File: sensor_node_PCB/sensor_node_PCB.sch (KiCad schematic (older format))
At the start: 37 parts, among them J1 USB_B_Mini, J3 OUTPUT_CONNECTOR, P1 BREAKOUTS, Q1 FDN340P, Q2 BSS138, Q3 BSS138, U1 LMV358IDGKR, U10 dps310, U2 LD1117S50TR, U4 LM1117-3.3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

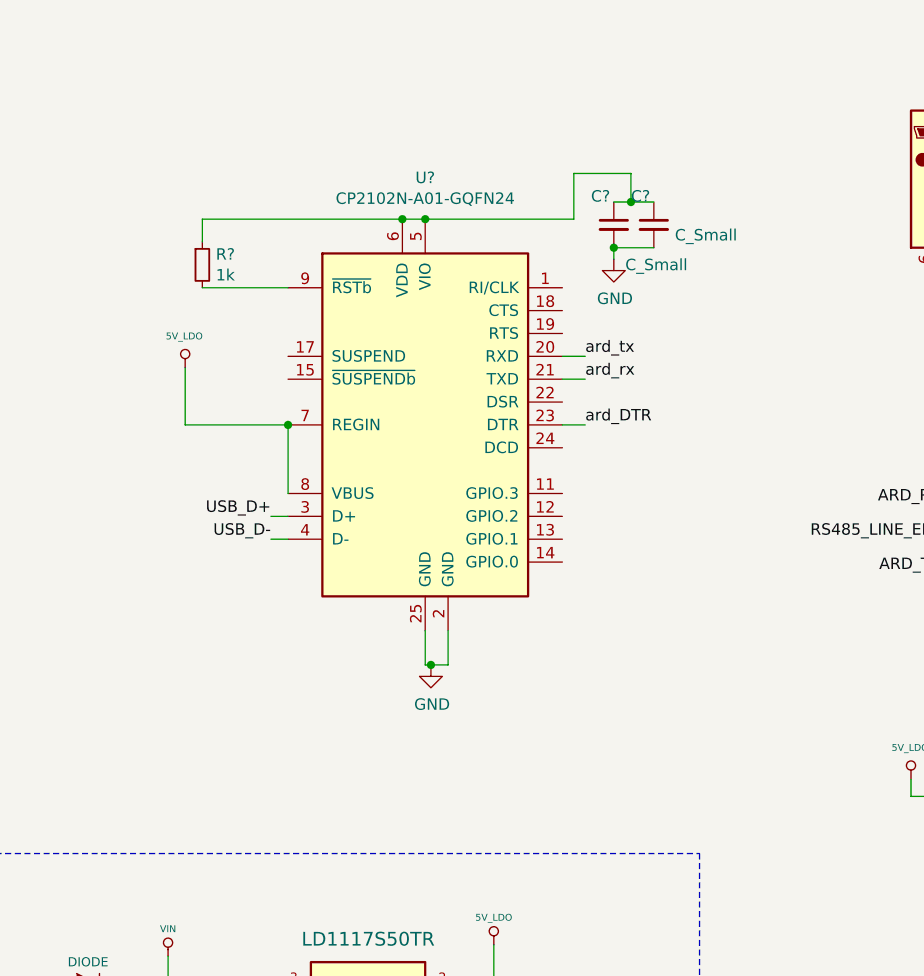
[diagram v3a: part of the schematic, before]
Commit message: changed cp2102 to 28 pin version
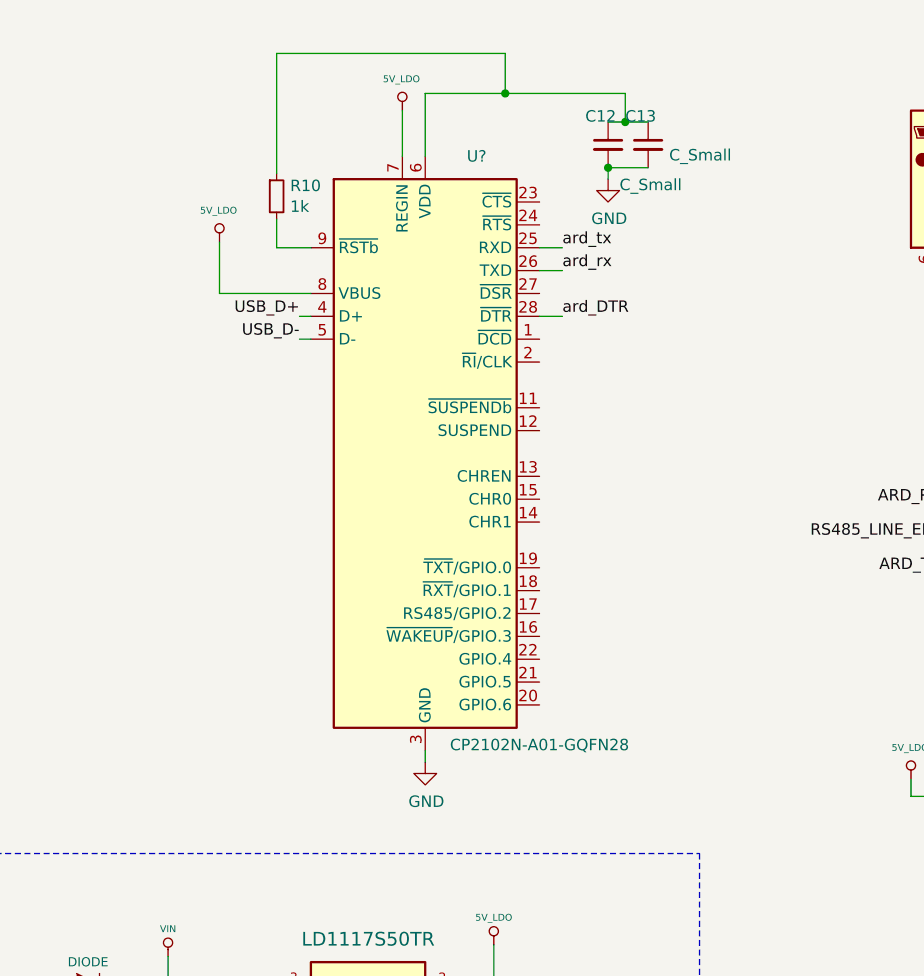
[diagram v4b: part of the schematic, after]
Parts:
- removed U?: CP2102N-A01-GQFN24, Package_DFN_QFN:QFN-24-1EP_4x4mm_P0.5mm_EP2.6x2.6mm, symbol Interface_USB:CP2102N-A01-GQFN24
- added U?: CP2102N-A01-GQFN28, Package_DFN_QFN:QFN-28-1EP_5x5mm_P0.5mm_EP3.35x3.35mm, symbol Interface_USB:CP2102N-A01-GQFN28
- C12, C13: renamed from C?; footprint (none) -> Capacitor_SMD:C_0603_1608Metric
- R10: renamed from R?; footprint (none) -> Resistor_SMD:R_0603_1608Metric
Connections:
- net 5V_LDO: now also U?.7 (REGIN), U?.8 (VBUS)
- net GND: now also U?.29 (GND), U?.3 (GND)
- net USB_D+: now also U?.4 (D+)
- net USB_D-: now also U?.5 (D-)
- net ard_DTR: now also U?.28 (~DTR)
- net ard_rx: now also U?.26 (TXD)
- net ard_tx: now also U?.25 (RXD)
- net at C12.1, C13.1, R10.1: now also U?.6 (VDD)
- net at R10.2: now also U?.9 (~RSTb)
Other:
- moved on the sheet: C12, C13, R10
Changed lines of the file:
@@
 Text GLabel 1800 4725 0    50   Input ~ 0
 12V_BUS
-Text Label 3275 2675 2    50   ~ 0
+Text Label 3400 1800 2    50   ~ 0
 USB_D+
-Text Label 3275 2775 2    50   ~ 0
+Text Label 3400 1900 2    50   ~ 0
 USB_D-
 Text Label 1425 3150 0    50   ~ 0
@@
 Wire Wire Line
 	1350 3250 1425 3250
-Text Label 4650 1975 0    50   ~ 0
+Text Label 4550 1500 0    50   ~ 0
 ard_tx
-Text Label 4650 2075 0    50   ~ 0
+Text Label 4550 1600 0    50   ~ 0
 ard_rx
 Text Label 1450 3050 0    50   ~ 0
 ard_DTR
-Text Label 4650 2275 0    50   ~ 0
+Text Label 4550 1800 0    50   ~ 0
 ard_DTR
-$Comp
-L Arduino_Uno_R3_From_Scratch-rescue:GND #PWR0112
-U 1 1 5F50BD57
-P 3975 3325
-F 0 "#PWR0112" H 3975 3075 50  0001 C CNN
-F 1 "GND" H 3980 3152 50  0000 C CNN
-F 2 "" H 3975 3325 60  0000 C CNN
-F 3 "" H 3975 3325 60  0000 C CNN
-	1    3975 3325
-	1    0    0    -1
-$EndComp
 Text Label 1425 2675 0    50   ~ 0
 ARD_TX1
@@
 Connection ~ 7075 5600
 $Comp
-L Interface_USB:CP2102N-A01-GQFN24 U?
-U 1 1 5FEADE93
-P 3950 2275
-F 0 "U?" H 3950 3356 50  0000 C CNN
-F 1 "CP2102N-A01-GQFN24" H 3950 3265 50  0000 C CNN
-F 2 "Package_DFN_QFN:QFN-24-1EP_4x4mm_P0.5mm_EP2.6x2.6mm" H 4400 1475 50  0001 L CNN
-F 3 "https://www.silabs.com/documents/public/data-sheets/cp2102n-datasheet.pdf" H 4000 1225 50  0001 C CNN
-	1    3950 2275
-	1    0    0    -1
-$EndComp
+L Arduino_Uno_R3_From_Scratch-rescue:5V_LDO #PWR0111
+U 1 1 5FEB97F5
+P 3850 900
+F 0 "#PWR0111" H 3850 990 20  0001 C CNN
+F 1 "5V_LDO" H 3846 1038 30  0000 C CNN
+F 2 "" H 3850 900 60  0000 C CNN
+F 3 "" H 3850 900 60  0000 C CNN
+	1    3850 900
+	1    0    0    -1
+$EndComp
+$Comp
+L Device:R_Small R10
+U 1 1 5FF181DD
+P 3300 1275
+F 0 "R10" H 3359 1321 50  0000 L CNN
+F 1 "1k" H 3359 1230 50  0000 L CNN
+F 2 "Resistor_SMD:R_0603_1608Metric" H 3300 1275 50  0001 C CNN
+F 3 "~" H 3300 1275 50  0001 C CNN
+	1    3300 1275
+	1    0    0    -1
+$EndComp
+$Comp
+L Device:C_Small C12
+U 1 1 5FF3FE64
+P 4750 1050
+F 0 "C12" H 4650 1175 50  0000 L CNN
+F 1 "C_Small" H 4800 875 50  0000 L CNN
+F 2 "Capacitor_SMD:C_0603_1608Metric" H 4750 1050 50  0001 C CNN
+F 3 "~" H 4750 1050 50  0001 C CNN
+	1    4750 1050
+	1    0    0    -1
+$EndComp
+$Comp
+L Device:C_Small C13
+U 1 1 5FF40686
+P 4925 1050
+F 0 "C13" H 4825 1175 50  0000 L CNN
+F 1 "C_Small" H 5017 1005 50  0000 L CNN
+F 2 "Capacitor_SMD:C_0603_1608Metric" H 4925 1050 50  0001 C CNN
+F 3 "~" H 4925 1050 50  0001 C CNN
+	1    4925 1050
+	1    0    0    -1
+$EndComp
+Wire Wire Line
+	4825 825  4825 950
+Wire Wire Line
+	4825 950  4750 950
+Wire Wire Line
+	4825 950  4925 950
+Connection ~ 4825 950
+Wire Wire Line
+	4925 1150 4750 1150
+Wire Wire Line
+	4750 1150 4750 1200
+Connection ~ 4750 1150
+$Comp
+L Arduino_Uno_R3_From_Scratch-rescue:GND #PWR0146
+U 1 1 5FF6DE1E
+P 4750 1200
+F 0 "#PWR0146" H 4750 950 50  0001 C CNN
+F 1 "GND" H 4755 1027 50  0000 C CNN
+F 2 "" H 4750 1200 60  0000 C CNN
+F 3 "" H 4750 1200 60  0000 C CNN
+	1    4750 1200
+	1    0    0    -1
+$EndComp
+$Comp
+L Interface_USB:CP2102N-A01-GQFN28 U?
+U 1 1 5FF9F30A
+P 3950 2400
+F 0 "U?" H 4175 3700 50  0000 C CNN
+F 1 "CP2102N-A01-GQFN28" H 4450 1125 50  0000 C CNN
+F 2 "Package_DFN_QFN:QFN-28-1EP_5x5mm_P0.5mm_EP3.35x3.35mm" H 4400 1200 50  0001 L CNN
+F 3 "https://www.silabs.com/documents/public/data-sheets/cp2102n-datasheet.pdf" H 4000 1650 50  0001 C CNN
+	1    3950 2400
+	1    0    0    -1
+$EndComp
+Wire Wire Line
+	3450 1500 3300 1500
+Wire Wire Line
+	3300 1500 3300 1375
 $Comp
 L Arduino_Uno_R3_From_Scratch-rescue:5V_LDO #PWR?
-U 1 1 5FEB97F5
-P 2900 2025
-F 0 "#PWR?" H 2900 2115 20  0001 C CNN
-F 1 "5V_LDO" H 2896 2163 30  0000 C CNN
-F 2 "" H 2900 2025 60  0000 C CNN
-F 3 "" H 2900 2025 60  0000 C CNN
-	1    2900 2025
-	1    0    0    -1
-$EndComp
-Wire Wire Line
-	2900 2025 2900 2275
-Wire Wire Line
-	2900 2275 3350 2275
-Wire Wire Line
-	3950 3175 3950 3325
-Wire Wire Line
-	3950 3325 3975 3325
-Wire Wire Line
-	4050 3175 4050 3325
-Wire Wire Line
-	4050 3325 3975 3325
-Connection ~ 3975 3325
-Wire Wire Line
-	4550 2275 4650 2275
-Wire Wire Line
-	4550 1975 4650 1975
-Wire Wire Line
-	4550 2075 4650 2075
-Wire Wire Line
-	3275 2675 3350 2675
-Wire Wire Line
-	3275 2775 3350 2775
-Wire Wire Line
-	3950 1375 3850 1375
-$Comp
-L Device:R_Small R?
-U 1 1 5FF181DD
-P 2975 1575
-F 0 "R?" H 3034 1621 50  0000 L CNN
-F 1 "1k" H 3034 1530 50  0000 L CNN
-F 2 "" H 2975 1575 50  0001 C CNN
-F 3 "~" H 2975 1575 50  0001 C CNN
-	1    2975 1575
-	1    0    0    -1
-$EndComp
-Wire Wire Line
-	2975 1675 3350 1675
-Wire Wire Line
-	2975 1375 3850 1375
-Wire Wire Line
-	2975 1375 2975 1475
-Connection ~ 3850 1375
-Wire Wire Line
-	3350 2575 3350 2275
-Connection ~ 3350 2275
-$Comp
-L Device:C_Small C?
-U 1 1 5FF3FE64
-P 4775 1400
-F 0 "C?" H 4675 1525 50  0000 L CNN
-F 1 "C_Small" H 4825 1225 50  0000 L CNN
-F 2 "" H 4775 1400 50  0001 C CNN
-F 3 "~" H 4775 1400 50  0001 C CNN
-	1    4775 1400
-	1    0    0    -1
-$EndComp
-$Comp
-L Device:C_Small C?
-U 1 1 5FF40686
-P 4950 1400
-F 0 "C?" H 4850 1525 50  0000 L CNN
-F 1 "C_Small" H 5042 1355 50  0000 L CNN
-F 2 "" H 4950 1400 50  0001 C CNN
-F 3 "~" H 4950 1400 50  0001 C CNN
-	1    4950 1400
-	1    0    0    -1
-$EndComp
-Wire Wire Line
-	3950 1375 4600 1375
-Wire Wire Line
-	4600 1375 4600 1175
-Wire Wire Line
-	4600 1175 4850 1175
-Wire Wire Line
-	4850 1175 4850 1300
-Wire Wire Line
-	4850 1300 4775 1300
-Connection ~ 3950 1375
-Wire Wire Line
-	4850 1300 4950 1300
-Connection ~ 4850 1300
-Wire Wire Line
-	4950 1500 4775 1500
-Wire Wire Line
-	4775 1500 4775 1550
-Connection ~ 4775 1500
+U 1 1 600093F3
+P 3050 1475
+F 0 "#PWR?" H 3050 1565 20  0001 C CNN
+F 1 "5V_LDO" H 3046 1613 30  0000 C CNN
+F 2 "" H 3050 1475 60  0000 C CNN
+F 3 "" H 3050 1475 60  0000 C CNN
+	1    3050 1475
+	1    0    0    -1
+$EndComp
+Wire Wire Line
+	3050 1475 3050 1700
+Wire Wire Line
+	3050 1700 3450 1700
+Wire Wire Line
+	3400 1800 3450 1800
+Wire Wire Line
+	3400 1900 3450 1900
+Wire Wire Line
+	3950 825  3950 1100
+Wire Wire Line
+	3950 825  4300 825
+Wire Wire Line
+	4550 1500 4450 1500
+Wire Wire Line
+	4450 1600 4550 1600
+Wire Wire Line
+	4450 1800 4550 1800
 $Comp
 L Arduino_Uno_R3_From_Scratch-rescue:GND #PWR?
-U 1 1 5FF6DE1E
-P 4775 1550
-F 0 "#PWR?" H 4775 1300 50  0001 C CNN
-F 1 "GND" H 4780 1377 50  0000 C CNN
-F 2 "" H 4775 1550 60  0000 C CNN
-F 3 "" H 4775 1550 60  0000 C CNN
-	1    4775 1550
-	1    0    0    -1
-$EndComp
+U 1 1 600955EC
+P 3950 3750
+F 0 "#PWR?" H 3950 3500 50  0001 C CNN
+F 1 "GND" H 3955 3577 50  0000 C CNN
+F 2 "" H 3950 3750 60  0000 C CNN
+F 3 "" H 3950 3750 60  0000 C CNN
+	1    3950 3750
+	1    0    0    -1
+$EndComp
+Wire Wire Line
+	3950 3750 3950 3700
+Wire Wire Line
+	3850 900  3850 1100
+Wire Wire Line
+	3300 650  4300 650
+Wire Wire Line
+	4300 650  4300 825
+Wire Wire Line
+	3300 650  3300 1175
+Connection ~ 4300 825
+Wire Wire Line
+	4300 825  4825 825
 $EndSCHEMATC

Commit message: got JSON parse working
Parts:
- gave numbers to parts that had none: 1
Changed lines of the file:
@@
 $EndComp
 $Comp
-L Interface_USB:CP2102N-A01-GQFN28 U?
+L Interface_USB:CP2102N-A01-GQFN28 U3
 U 1 1 5FF9F30A
 P 3950 2400
-F 0 "U?" H 4175 3700 50  0000 C CNN
+F 0 "U3" H 4175 3700 50  0000 C CNN
 F 1 "CP2102N-A01-GQFN28" H 4450 1125 50  0000 C CNN
 F 2 "Package_DFN_QFN:QFN-28-1EP_5x5mm_P0.5mm_EP3.35x3.35mm" H 4400 1200 50  0001 L CNN
@@
 	3300 1500 3300 1375
 $Comp
-L Arduino_Uno_R3_From_Scratch-rescue:5V_LDO #PWR?
+L Arduino_Uno_R3_From_Scratch-rescue:5V_LDO #PWR0112
 U 1 1 600093F3
 P 3050 1475
-F 0 "#PWR?" H 3050 1565 20  0001 C CNN
+F 0 "#PWR0112" H 3050 1565 20  0001 C CNN
 F 1 "5V_LDO" H 3046 1613 30  0000 C CNN
 F 2 "" H 3050 1475 60  0000 C CNN
@@
 	4450 1800 4550 1800
 $Comp
-L Arduino_Uno_R3_From_Scratch-rescue:GND #PWR?
+L Arduino_Uno_R3_From_Scratch-rescue:GND #PWR0148
 U 1 1 600955EC
 P 3950 3750
-F 0 "#PWR?" H 3950 3500 50  0001 C CNN
+F 0 "#PWR0148" H 3950 3500 50  0001 C CNN
 F 1 "GND" H 3955 3577 50  0000 C CNN
 F 2 "" H 3950 3750 60  0000 C CNN
